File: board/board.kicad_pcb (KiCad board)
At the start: 2 copper layers, 45 x 13 mm, 18 parts, among them J1 007_ADC, J2 Conn_01x02_Male, J3 007_ADC, U1 TCA0372

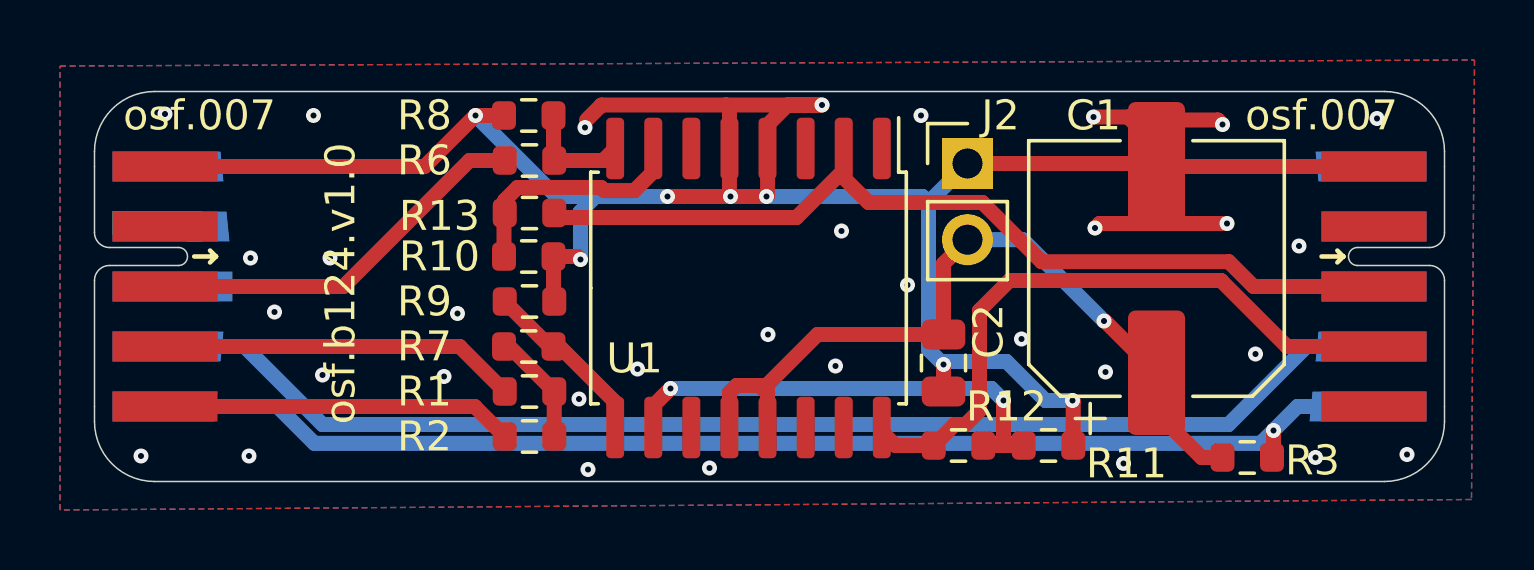
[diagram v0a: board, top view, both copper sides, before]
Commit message: added missing schemetic
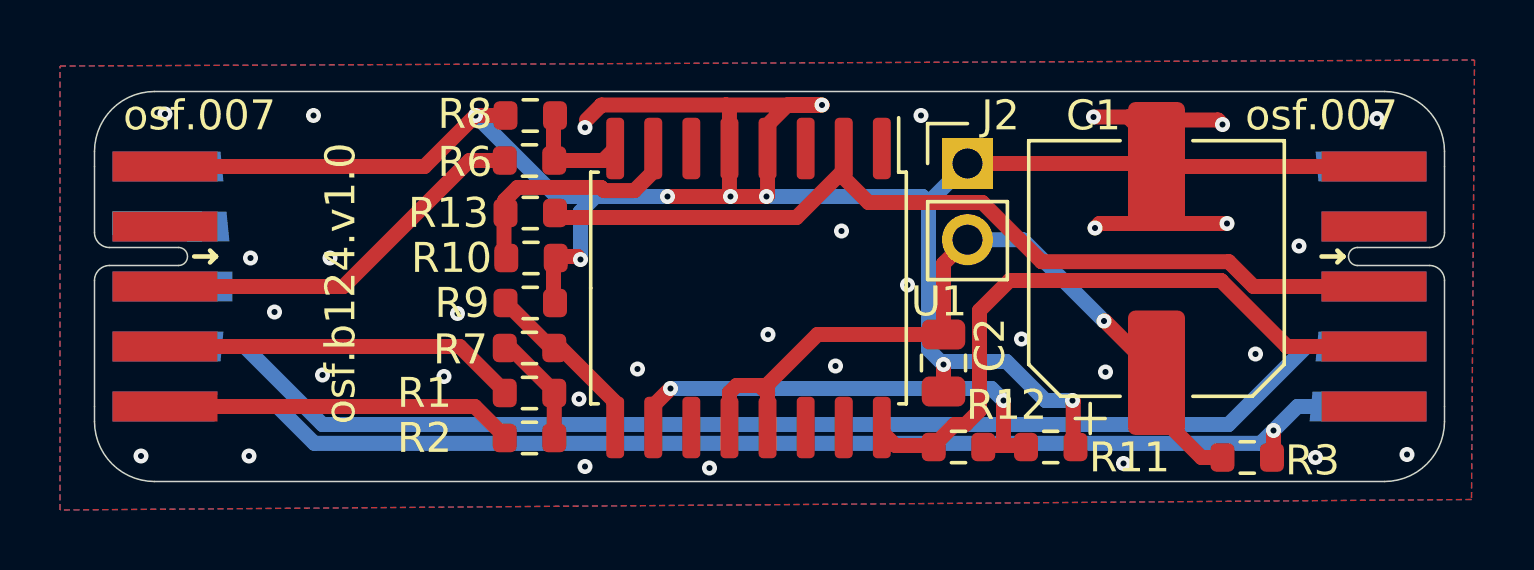
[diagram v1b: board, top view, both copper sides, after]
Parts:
- moved R10 0.09 mm to (153.8, 94.2)
- moved R11 0.09 mm to (171.1, 100.5)
- moved R9 0.06 mm to (153.7, 95.7)
- moved R7 0.06 mm to (153.7, 97.2)
- moved R1 0.05 mm to (153.7, 98.7)
- moved R2 0.05 mm to (153.7, 100.2)
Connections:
- net /implementation/in1 renamed /amp/in1
- net /implementation/in2 renamed /amp/in2
- net /implementation/out1 renamed /amp/out1
- net /implementation/out2 renamed /amp/out2
